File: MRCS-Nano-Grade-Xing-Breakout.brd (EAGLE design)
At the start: 99.8 x 68.8 mm, 26 parts, among them M2 SMALL_SERVO

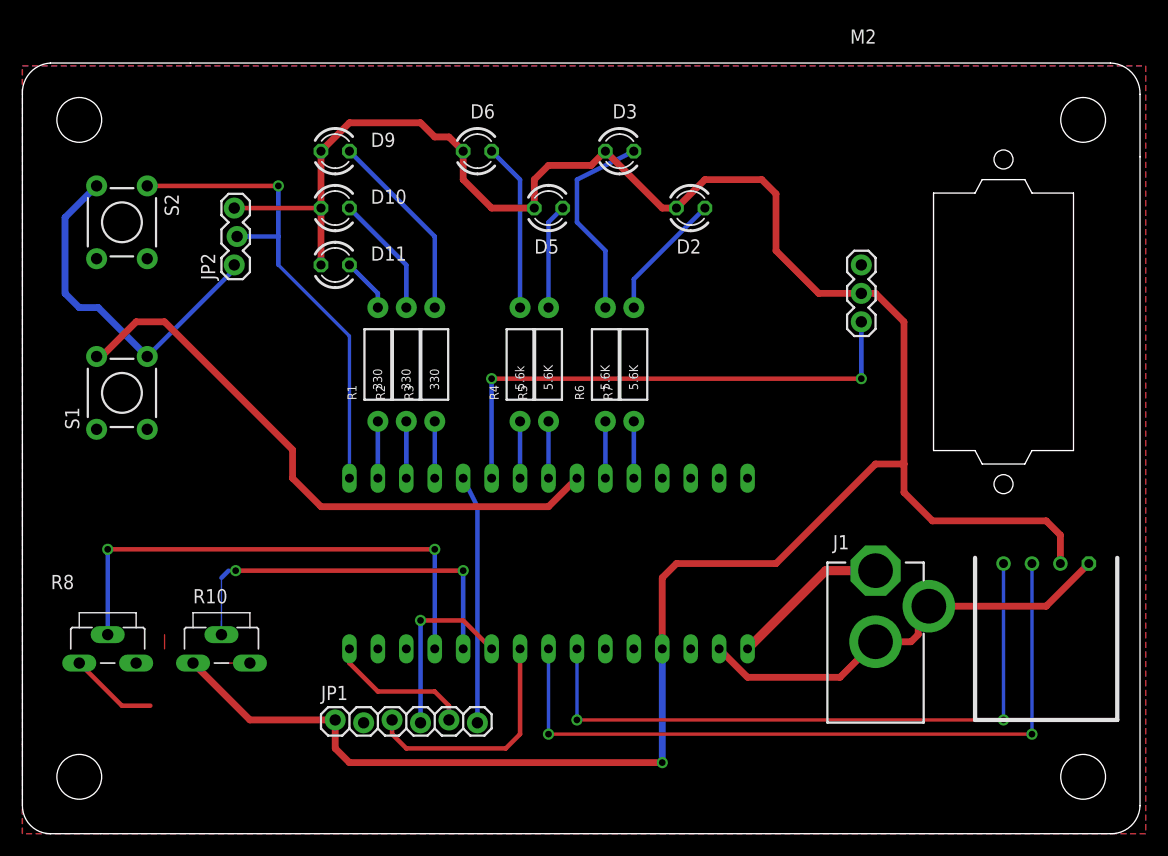
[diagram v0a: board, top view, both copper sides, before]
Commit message: completed initial deisgn
After some consultation with Jon Schmidt this is ready to try for fab
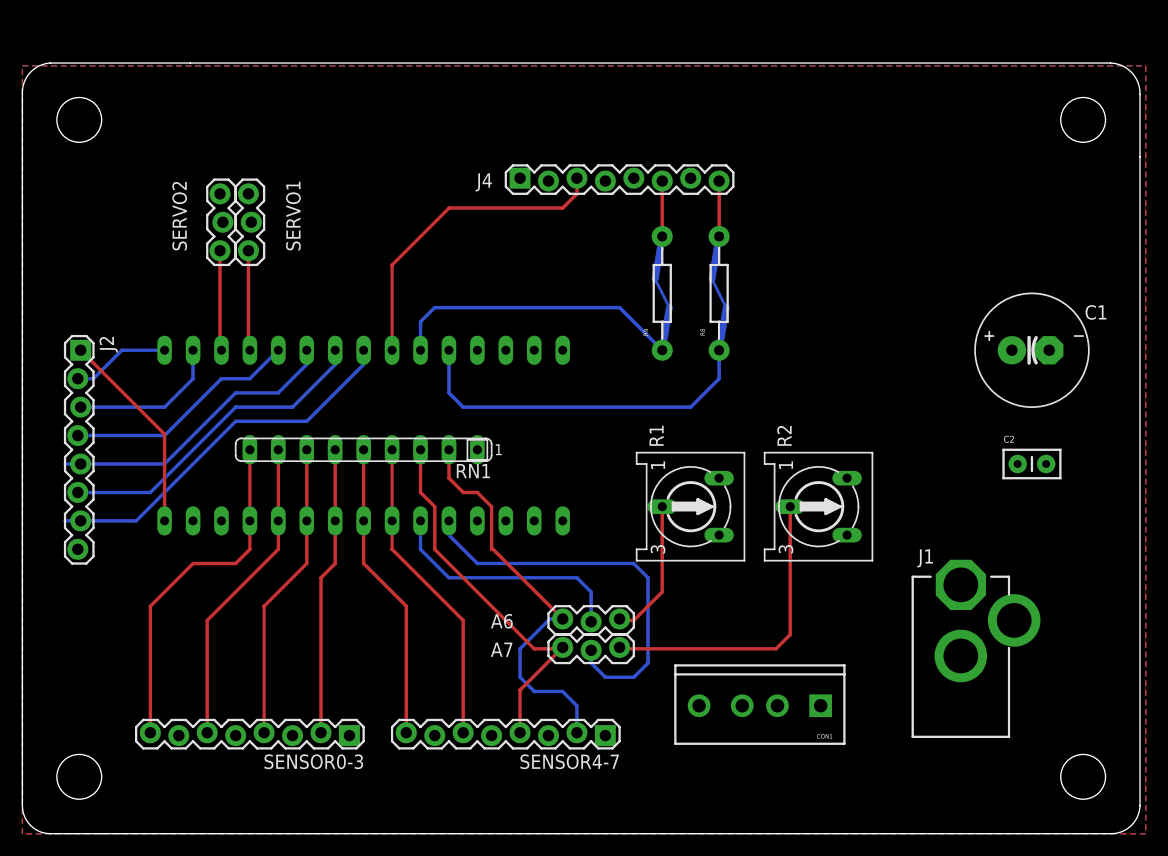
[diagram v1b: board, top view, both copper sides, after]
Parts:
- removed D10: Yellow, SPCoast:LED3MM
- removed D11: Red, SPCoast:LED3MM
- removed D2, D3, D5, D6: White, SPCoast:LED3MM
- removed D9: Green, SPCoast:LED3MM
- removed JP1: (no value), SparkFun-Connectors:1X06_LOCK
- removed JP2: (no value), SparkFun-Connectors:1X03_LOCK
- removed M2: SMALL_SERVO, SparkFun-Electromechanical:1X03
- removed R10: BOURNS_3306W, mschutzer:BOURNS_3306W
- removed R3: 330, SparkFun-Resistors:AXIAL-0.4
- removed R4: 5.6k, SparkFun-Resistors:AXIAL-0.4
- removed R5, R6, R7: 5.6K, SparkFun-Resistors:AXIAL-0.4
- removed S1, S2: SWITCH-MOMENTARY-2PTH, SparkFun-Electromechanical:TACTILE-PTH
- removed U$11: (no value), SPCoast:SERVO-9G
- removed U$9: I2CRA, SPCoast-minimal:I2C
- added A6, A7, SERVO1, SERVO2: (no value), SparkFun-Connectors:1X03_LOCK
- added C1: 470 uF @ 16V, SPCoast:E3.5-10
- added C2: .1 @ 25V, SPCoast:C-PTH-0.100
- added CON1: 5V PWR, SPCoast:SCREWTERMINAL-3.5MM-4_LOCK
- added J2: Unused I/O, SPCoast:1X08_LOCK
- added J4: Outputs, SPCoast:1X08_LOCK
- added R9: (no value), SPCoast:CUT-R
- added RN1: 4700, resistor-sil:SIL9
- added SENSOR0-3, SENSOR4-7: (no value), SPCoast:1X08_LOCK
- added U$2: (no value), MRCS-prop65warningBtm:CA-PROP65WARNING
- J1: value (none) -> 5V PWR
- R1, R2: value 330 -> 10K; device SparkFun-Resistors:AXIAL-0.4 -> pot:RS3
- R8: value BOURNS_3306W -> (none); device mschutzer:BOURNS_3306W -> SPCoast:CUT-R
- moved R8 63.8 mm to (62.2, 48.3), turned to 90 degrees
- moved R2 39.0 mm to (71.1, 29.2), turned to 270 degrees
- moved R1 30.7 mm to (59.7, 29.2), turned to 270 degrees
- moved U$1 20.1 mm to (39.4, 38.1)
- moved J1 7.73 mm to (83.8, 19.1)
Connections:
- removed net A1: R10.2, U$1.A1
- removed net D10: R2.P$1, U$1.D10
- removed net D11: R1.P$1, U$1.D11
- removed net D12: JP2.2, S2.1, U$1.D12
- removed net D2: R7.P$1, U$1.D2
- removed net D3: R6.P$1, U$1.D3
- removed net D5: R5.P$1, U$1.D5
- removed net D6: R4.P$1, U$1.D6
- removed net D7: M2.1, U$1.D7
- removed net D9: R3.P$1, U$1.D9
- removed net SCL: U$1.A5, U$9.SCL
- removed net SDA: U$1.A4, U$9.SDA
- new net N$14: A6.3, R1.S
- new net N$15: A6.2, U$1.A6
- new net N$16: A7.2, U$1.A7
- new net N$17: RN1.8, SENSOR0-3.6, U$1.A1
- new net N$18: A7.3, R2.S
- new net N$19: J2.1, U$1.D13
- new net N$20: J2.2, U$1.D12
- new net N$21: J2.3, U$1.D11
- new net N$22: J2.4, U$1.D8
- new net N$23: J2.5, U$1.D7
- new net N$24: J2.6, U$1.D6
- new net N$25: J2.7, U$1.D5
- net 5V: now also C1.+, C2.1, CON1.2, CON1.4, J1.1, J4.1, J4.5, J4.7, R1.E, R2.E, SENSOR0-3.1, SENSOR0-3.3, SENSOR0-3.5, SENSOR0-3.7, SENSOR4-7.1, SENSOR4-7.3, SENSOR4-7.5, SENSOR4-7.7, SERVO1.2, SERVO2.2; no longer D10.A, D11.A, D2.A, D3.A, D5.A, D6.A, D9.A, JP1.1, JP2.3, M2.2, R10.3, R8.3, U$9.V+
- net A0: now also RN1.9, SENSOR0-3.8; no longer R8.2
- net GND: now also C1.-, C2.2, CON1.1, CON1.3, J2.8, J4.2, J4.4, R1.A, R2.A, RN1.1, SERVO1.3, SERVO2.3; no longer JP1.2, JP2.1, M2.3, R10.1, R8.1, S1.1, S2.3, U$9.GND
- net N$1: now also RN1.5, SENSOR4-7.8, U$1.A4; no longer J1.1, U$1.RAW
- net N$10: now also RN1.7, SENSOR0-3.4, U$1.A2; no longer JP1.5, U$1.D13
- net N$11: now also A7.1, RN1.3, SENSOR4-7.4; no longer JP1.6, U$1.D8
- net N$12: now also RN1.6, SENSOR0-3.2, U$1.A3; no longer JP1.4, U$1.A2
- net N$13: now also A6.1, RN1.2, SENSOR4-7.2; no longer JP1.3, U$1.A3
- net N$2: now also R8.P2, U$1.D2; no longer D11.K, R1.P$2
- net N$3: now also J4.8, R8.P1; no longer D10.K, R2.P$2
- net N$4: now also R9.P2, U$1.D3; no longer D9.K, R3.P$2
- net N$5: now also J4.6, R9.P1; no longer D6.K, R4.P$2
- net N$6: now also J4.3, U$1.D4; no longer D5.K, R5.P$2
- net N$7: now also RN1.4, SENSOR4-7.6, U$1.A5; no longer D3.K, R6.P$2
- net N$8: now also SERVO2.1, U$1.D10; no longer D2.K, R7.P$2
- net N$9: now also SERVO1.1, U$1.D9; no longer S1.3, U$1.D4
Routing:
- net 5V: track 221.3 -> 0.00 mm, vias 1 -> 0
- net GND: track 75.1 -> 0.00 mm
- net SDA: track 66.0 -> 0.00 mm, vias 2 -> 0
- net SCL: track 58.4 -> 0.00 mm, vias 2 -> 0
- net D7: track 47.0 -> 0.00 mm, vias 2 -> 0
- net N$9: track 53.6 -> 8.94 mm
- net D12: track 44.1 -> 0.00 mm, vias 1 -> 0
- net N$16: track 0.00 -> 35.5 mm
- net A1: track 35.2 -> 0.00 mm, vias 2 -> 0
- net N$25: track 0.00 -> 33.7 mm
- net N$24: track 0.00 -> 29.0 mm
- net N$17: track 0.00 -> 28.0 mm
- net N$18: track 0.00 -> 27.2 mm
- net N$2: track 4.86 -> 32.1 mm
- net N$23: track 0.00 -> 26.5 mm
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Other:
- board text added: "+GBG+L+L 5NLN5152"
- board text added: "0+1+2+3+"
- board text added: "4+5+6+7+"
- board text added: "5DVC"
- board text added: "5G5G"
- board text added: "Grade XING Breakout"
- board text added: "Seth Neumann Jon Schmidt"
- board text added: "V1.0 20200314"
- board text removed: "3 pin module"
- board text removed: "5V"
- board text removed: "A0"
- board text removed: "A1"
- board text removed: "A2"
- board text removed: "A3"
- board text removed: "D12"
- board text removed: "D13"
- board text removed: "D4"
- board text removed: "D7"
- board text removed: "D8"
- board text removed: "Earl Girbovan"
- board text removed: "GND"
- board text removed: "Model Railroading is fun!"
- board text removed: "PCR Arduino Clinic - 2017"
- board text removed: "Seth Neumann John Plocher"
- board text removed: "Solder Side"
- board text removed: "V4.0 20190408"
